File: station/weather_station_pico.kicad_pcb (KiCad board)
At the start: 2 copper layers, 75.1 x 75 mm, 24 parts, among them J2 STEMMA_QT, J3 73412-0110, J4 STEMMA, J5 RJ11, J6 RJ11, J7 DS18B20, J8 Battery Charger, U1 Pico, U2 RFM69, U3 APDS_LightSensor

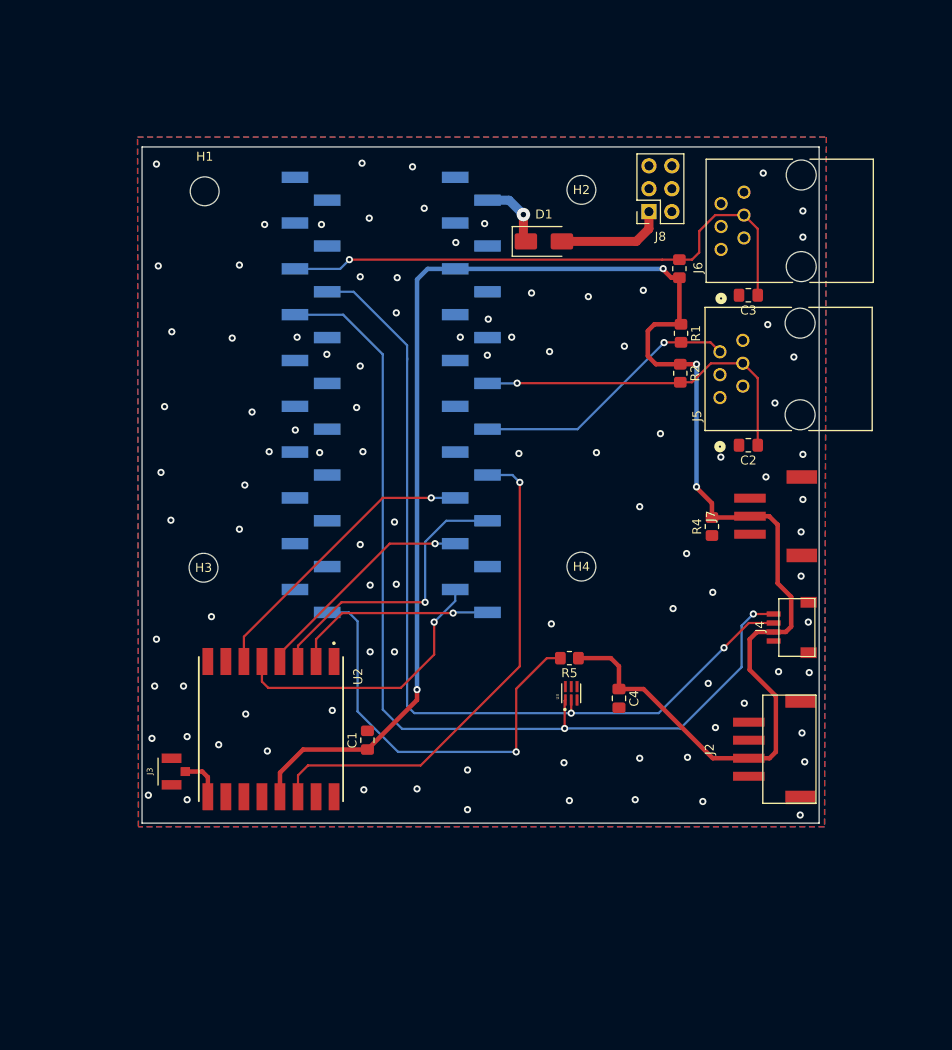
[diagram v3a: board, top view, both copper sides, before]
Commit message: Switched to a round board
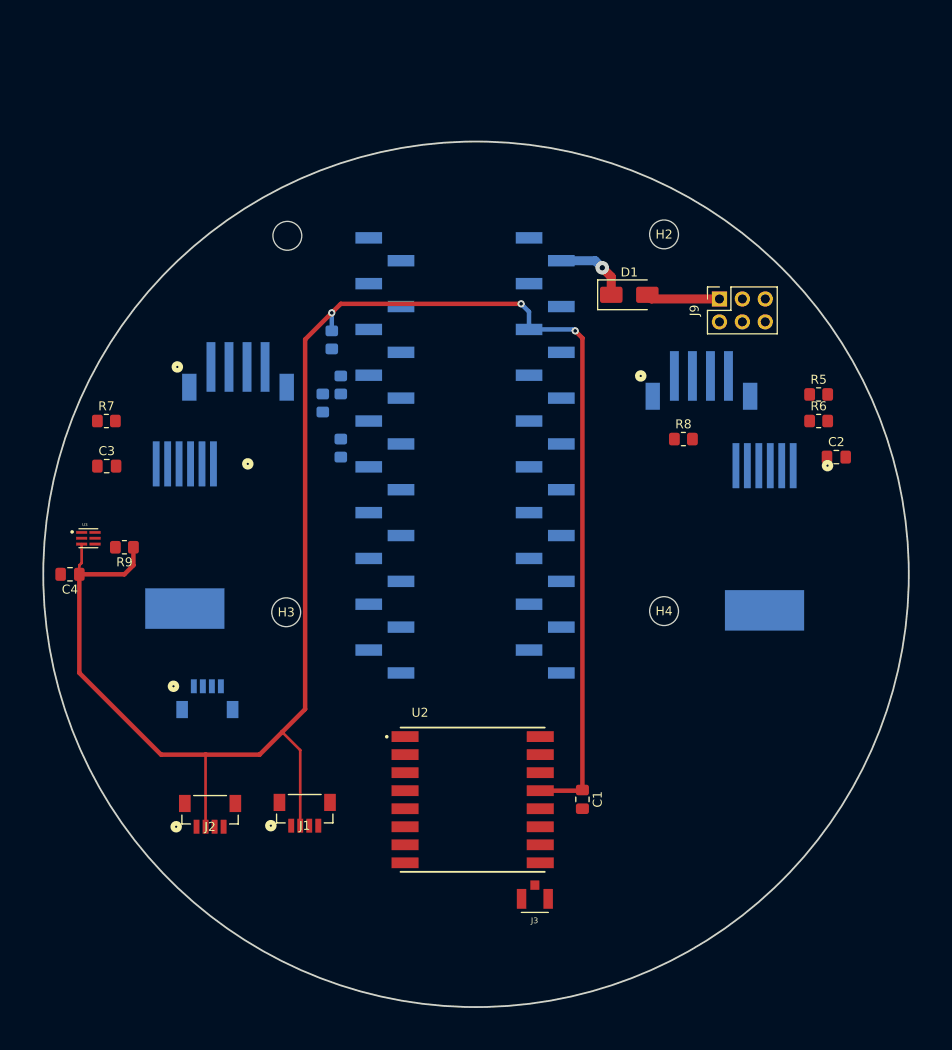
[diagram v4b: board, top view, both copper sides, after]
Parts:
- added J1: I2C1_EXP, WeatherStation:StemmaQT_Vertical, F.Cu at (128.4, 132.9)
- added J9: Battery Charger, Connector_PinSocket_2.54mm:PinSocket_2x03_P2.54mm_Vertical, F.Cu at (174.4, 76.4)
- added R6: 10K, Resistor_SMD:R_0805_2012Metric_Pad1.20x1.40mm_HandSolder, F.Cu at (185.4, 89.9)
- added R7: 10K, Resistor_SMD:R_0805_2012Metric_Pad1.20x1.40mm_HandSolder, F.Cu at (106.4, 89.9)
- added R8: 4.7k, Resistor_SMD:R_0805_2012Metric_Pad1.20x1.40mm_HandSolder, F.Cu at (170.4, 91.9)
- added R9: 10k, Resistor_SMD:R_0805_2012Metric_Pad1.20x1.40mm_HandSolder, F.Cu at (108.4, 103.9)
- J2: value STEMMA_QT -> I2C1_EXP; footprint WeatherStation:STEMMA_LARGE -> WeatherStation:StemmaQT_Vertical
- J4: value STEMMA -> BME280; footprint WeatherStation:STEMMA_SMALL -> WeatherStation:StemmaQT_Vertical; moved to B.Cu
- J5: value RJ11 -> WIND_SENSOR; footprint WeatherStation:CONN6_5555165-1_TEC -> WeatherStation:RJ11_SMD; moved to B.Cu
- J6: value RJ11 -> RAIN_SENSOR; footprint WeatherStation:CONN6_5555165-1_TEC -> WeatherStation:RJ11_SMD; moved to B.Cu
- J7: value DS18B20 -> SOIL_MOISTURE; footprint WeatherStation:STEMMA_LARGE_3pin -> WeatherStation:Stemma_Vertical_Large; moved to B.Cu
- J8: value Battery Charger -> SOIL_TEMP; footprint Connector_PinSocket_2.54mm:PinSocket_2x03_P2.54mm_Vertical -> WeatherStation:Stemma_Vertical_Large; moved to B.Cu
- R1, R2, R3: value 10K -> DNP; moved to B.Cu
- R4: value 4.7k -> DNP; moved to B.Cu
- R5: value 10k -> 10K
- U3: value APDS_LightSensor -> LIGHT_SENSOR
- moved C3 73.6 mm to (106.5, 94.9), turned to 0 degrees
- moved J6 67.4 mm to (115.1, 102.5), turned to 180 degrees
- moved J4 64.1 mm to (117.6, 121.2), turned to 0 degrees
- moved C4 62.4 mm to (102.4, 106.9), turned to 180 degrees
- moved J2 61.9 mm to (117.9, 133.0), turned to 0 degrees
- moved J7 60.5 mm to (121.0, 85.2), turned to 180 degrees
- moved U3 56.2 mm to (104.4, 102.9), turned to 0 degrees
- moved J3 42.7 mm to (154.0, 142.9), turned to 180 degrees
- moved R3 42.3 mm to (130.4, 87.9), turned to -90 degrees
- moved R4 42.1 mm to (132.4, 92.9)
- moved R5 40.2 mm to (185.4, 87.0), turned to 0 degrees
- moved R1 38.7 mm to (131.4, 80.9)
- moved R2 37.7 mm to (132.4, 85.9), turned to 90 degrees
- moved C1 24.7 mm to (159.2, 131.9), turned to -90 degrees
- moved U2 23.7 mm to (147.1, 131.9), turned to 0 degrees
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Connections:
- J2 pad 3: /I2C1_SDA -> /I2C0_SDA
- J2 pad 4: /I2C1_SCL -> /I2C0_SCL
- J2 pad 5: GND -> (no net)
- J2 pad 6: GND -> (no net)
- J3 pad 3: GND -> (no net)
- J4 pad 5: GND -> (no net)
- J4 pad 6: GND -> (no net)
- J7 pad 1: /ONE_WIRE -> GND
- J7 pad 3: GND -> /I2C0_SDA
- J7 pad 4: GND -> /I2C0_SCL
- J7 pad 5: GND -> (no net)
- J8 pad 1: /Battery Charger/Load+ -> /ONE_WIRE
- J8 pad 2: GND -> +3.3V
- J8 pad 4: /Battery Charger/SET -> (no net)
- J8 pad 5: /Battery Charger/~{FAULT} -> (no net)
- J8 pad 6: /Battery Charger/~{CHRG} -> (no net)
- R1 pad 2: /WINDDIR_OUT -> /I2C0_SDA
- R2 pad 2: /WINDSPEED_TGR -> /I2C0_SCL
- R3 pad 2: /RAIN_COUNT -> /I2C1_SDA
- R4 pad 1: /ONE_WIRE -> +3.3V
- R4 pad 2: +3.3V -> /I2C1_SCL
- R5 pad 2: /LIGHT_INTR -> /WINDDIR_OUT
- U1 pad 10: unconnected-(U1-GP7-Pad10) -> /I2C1_SCL
- U1 pad 19: unconnected-(U1-GP14-Pad19) -> /ONE_WIRE
- U1 pad 9: unconnected-(U1-GP6-Pad9) -> /I2C1_SDA
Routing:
- net /I2C0_SCL: track 106.4 -> 0.00 mm, vias 2 -> 0
- net /I2C0_SDA: track 98.2 -> 0.00 mm, vias 2 -> 0
- net /RAIN_COUNT: track 63.3 -> 0.00 mm, vias 1 -> 0
- net /RFM69 Radio/RFM69_INTR: track 56.3 -> 0.00 mm, vias 1 -> 0
- net /LIGHT_INTR: track 46.5 -> 0.00 mm, vias 1 -> 0
- net /WINDSPEED_TGR: track 39.0 -> 0.00 mm, vias 1 -> 0
- net /RFM69 Radio/RFM69_RESET: track 32.6 -> 0.00 mm, vias 1 -> 0
- net /RFM69 Radio/RFM69_MOSI: track 32.4 -> 0.00 mm, vias 1 -> 0
- net /RFM69 Radio/RFM69_CS: track 31.9 -> 0.00 mm, vias 1 -> 0
- net /WINDDIR_OUT: track 30.2 -> 0.00 mm, vias 1 -> 0
- net /RFM69 Radio/RFM69_CLK: track 25.4 -> 0.00 mm, vias 1 -> 0
- net /RFM69 Radio/RFM69_MISO: track 22.7 -> 0.00 mm, vias 1 -> 0
- net +3.3V: track 200.3 -> 206.2 mm, vias 4 -> 3
- net Net-(U2-ANT): track 4.93 -> 0.00 mm
- net /Battery Charger/Load+: track 12.1 -> 8.19 mm
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- removed copper zone on B.Cu, net GND
- removed copper zone on F.Cu, net GND
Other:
- board size 75.1 x 75 mm -> 96 x 96 mm

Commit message: Finished Circular Layout
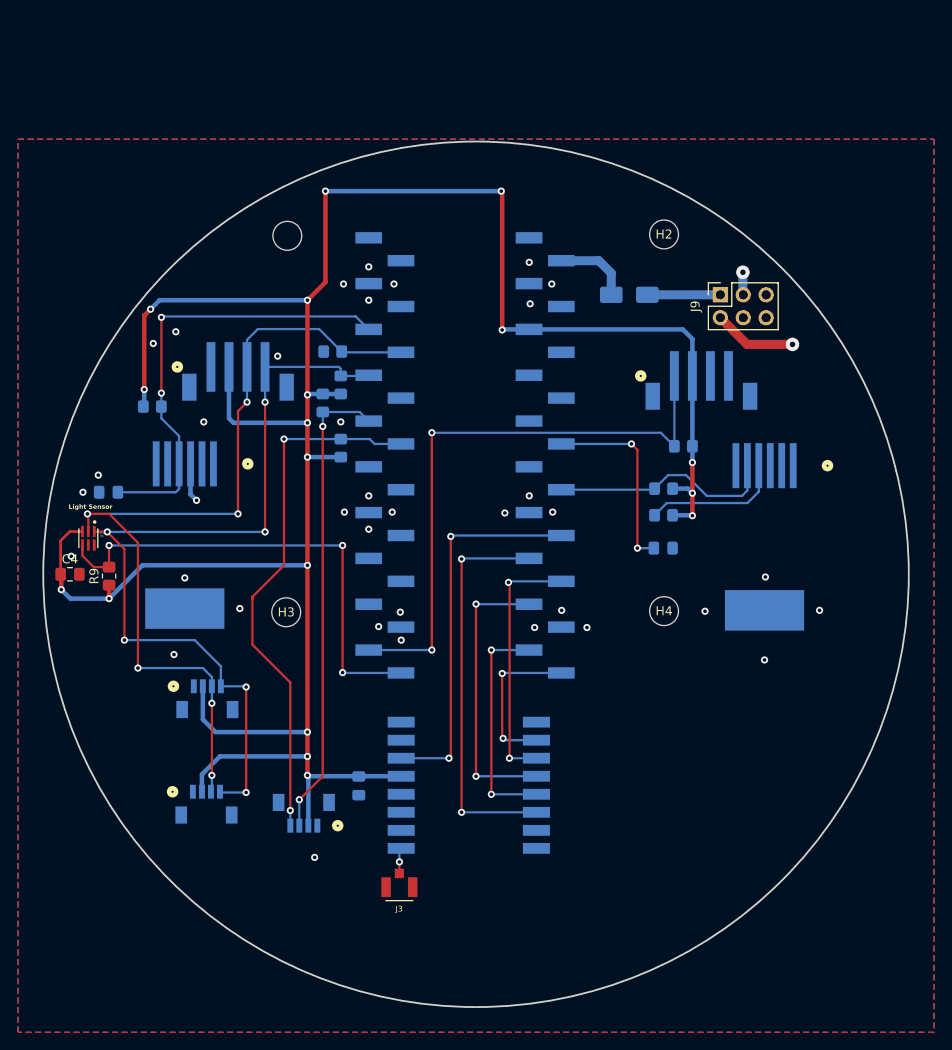
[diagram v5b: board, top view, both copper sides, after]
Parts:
- C1, C2, C3, D1, J1, R5, R6, R7, R8, U2: moved to B.Cu
- J2: value I2C1_EXP -> I2C0_EXP; moved to B.Cu
- moved C1 24.8 mm to (134.4, 130.4)
- moved C2 21.7 mm to (168.2, 104.0)
- moved R5 20.1 mm to (168.2, 97.4), turned to 180 degrees
- moved R6 20.1 mm to (168.2, 100.3), turned to 180 degrees
- moved J3 15.1 mm to (138.9, 141.6)
- moved R7 5.35 mm to (111.5, 88.3)
- moved R9 3.62 mm to (106.7, 107.1), turned to 90 degrees
- moved C3 2.91 mm to (106.7, 97.8), turned to 180 degrees
- moved U2 1.66 mm to (146.6, 130.3), turned to 180 degrees
- moved R1 1.30 mm to (131.5, 82.2), turned to 0 degrees
- moved R8 0.80 mm to (170.4, 92.7)
- moved J9 0.47 mm to (174.5, 75.9)
- moved J2 0.42 mm to (117.5, 132.9)
- moved J1 0.10 mm to (128.3, 132.9), turned to 180 degrees
- turned C4 to 0 degrees
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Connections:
- J1 pad 5: (no net) -> GND
- J1 pad 6: (no net) -> GND
- J2 pad 5: (no net) -> GND
- J2 pad 6: (no net) -> GND
- J3 pad 3: (no net) -> GND
- J4 pad 5: (no net) -> GND
- J4 pad 6: (no net) -> GND
- J5 pad 7: (no net) -> GND
- J6 pad 7: (no net) -> GND
- J8 pad 5: (no net) -> GND
- J8 pad 6: (no net) -> GND
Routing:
- net /I2C0_SDA: track 0.00 -> 99.3 mm, vias 0 -> 6
- net /I2C0_SCL: track 0.00 -> 94.1 mm, vias 0 -> 6
- net +3.3V: track 206.2 -> 282.6 mm, vias 3 -> 18
- net /ONE_WIRE: track 0.00 -> 66.4 mm, vias 0 -> 2
- net /I2C1_SCL: track 0.00 -> 59.3 mm, vias 0 -> 2
- net /LIGHT_INTR: track 0.00 -> 53.6 mm, vias 0 -> 3
- net /I2C1_SDA: track 0.00 -> 52.5 mm, vias 0 -> 2
- net /RAIN_COUNT: track 0.00 -> 50.4 mm, vias 0 -> 2
- net /RFM69 Radio/RFM69_RESET: track 0.00 -> 43.9 mm, vias 0 -> 2
- net /RFM69 Radio/RFM69_INTR: track 0.00 -> 42.3 mm, vias 0 -> 2
- net /WINDSPEED_TGR: track 0.00 -> 37.0 mm, vias 0 -> 2
- net /RFM69 Radio/RFM69_CLK: track 0.00 -> 31.7 mm, vias 0 -> 2
- net /RFM69 Radio/RFM69_MOSI: track 0.00 -> 28.5 mm, vias 0 -> 2
- net /WINDDIR_OUT: track 0.00 -> 25.3 mm
- net /RFM69 Radio/RFM69_CS: track 0.00 -> 25.2 mm, vias 0 -> 2
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- added copper zone on B.Cu, net GND
- added copper zone on F.Cu, net GND
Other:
- board text added: "Light Sensor"

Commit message: Finished Square layout
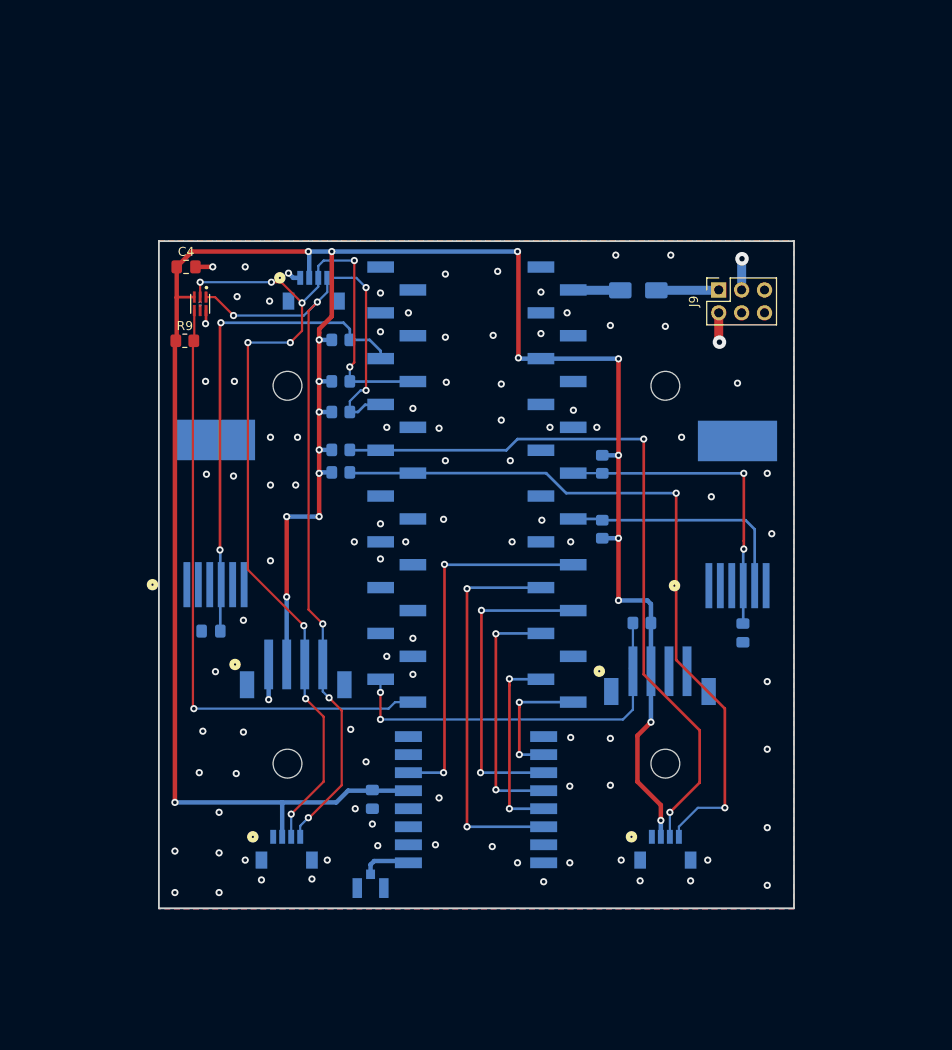
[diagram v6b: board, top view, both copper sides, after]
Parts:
- J3: moved to B.Cu
- moved H2 58.7 mm to (168.4, 127.9)
- moved H1 58.5 mm to (126.5, 127.9)
- moved J4 46.8 mm to (129.4, 75.9)
- moved J1 40.4 mm to (168.4, 137.9), turned to 0 degrees
- moved C4 36.4 mm to (115.3, 72.8)
- moved J7 33.6 mm to (127.4, 118.2)
- moved J8 33.1 mm to (167.8, 118.9)
- moved U3 28.8 mm to (116.8, 76.9)
- moved R9 27.4 mm to (115.1, 81.0), turned to 0 degrees
- moved H3 25.1 mm to (126.5, 86.0)
- moved H4 25.0 mm to (168.4, 86.0)
- moved R7 22.2 mm to (132.4, 80.9)
- moved R8 20.1 mm to (165.8, 112.3)
- moved C3 19.1 mm to (118.0, 113.2)
- moved C2 12.9 mm to (177.0, 113.4), turned to -90 degrees
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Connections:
- J1 pad 5: GND -> (no net)
- J1 pad 6: GND -> (no net)
- J2 pad 5: GND -> (no net)
- J2 pad 6: GND -> (no net)
- J3 pad 3: GND -> (no net)
- J4 pad 5: GND -> (no net)
- J4 pad 6: GND -> (no net)
- J5 pad 7: GND -> (no net)
- J6 pad 7: GND -> (no net)
- J8 pad 5: GND -> (no net)
- J8 pad 6: GND -> (no net)
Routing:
- net /I2C1_SDA: track 52.5 -> 81.2 mm
- net /ONE_WIRE: track 66.4 -> 43.0 mm
- net /I2C1_SCL: track 59.3 -> 81.4 mm
- net /LIGHT_INTR: track 53.6 -> 68.9 mm, vias 3 -> 1
- net /I2C0_SDA: track 99.3 -> 113.0 mm, vias 6 -> 10
- net /I2C0_SCL: track 94.1 -> 103.6 mm, vias 6 -> 7
- net +3.3V: track 282.6 -> 275.2 mm, vias 18 -> 19
- net /RFM69 Radio/RFM69_MOSI: track 28.5 -> 35.2 mm
- net /RAIN_COUNT: track 50.4 -> 54.8 mm
- net /RFM69 Radio/RFM69_CLK: track 31.7 -> 27.7 mm
- net /RFM69 Radio/RFM69_CS: track 25.2 -> 21.7 mm
- net Net-(D1-K): track 8.51 -> 5.24 mm
- net /RFM69 Radio/RFM69_MISO: track 17.6 -> 14.5 mm
- net Net-(U2-ANT): track 2.86 -> 5.52 mm, vias 1 -> 0
- net /WINDDIR_OUT: track 25.3 -> 26.9 mm
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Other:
- board size 96 x 96 mm -> 70.4 x 74 mm
- board text removed: "Light Sensor"

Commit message: Updated the I2C schematic for the soil moisture sensor
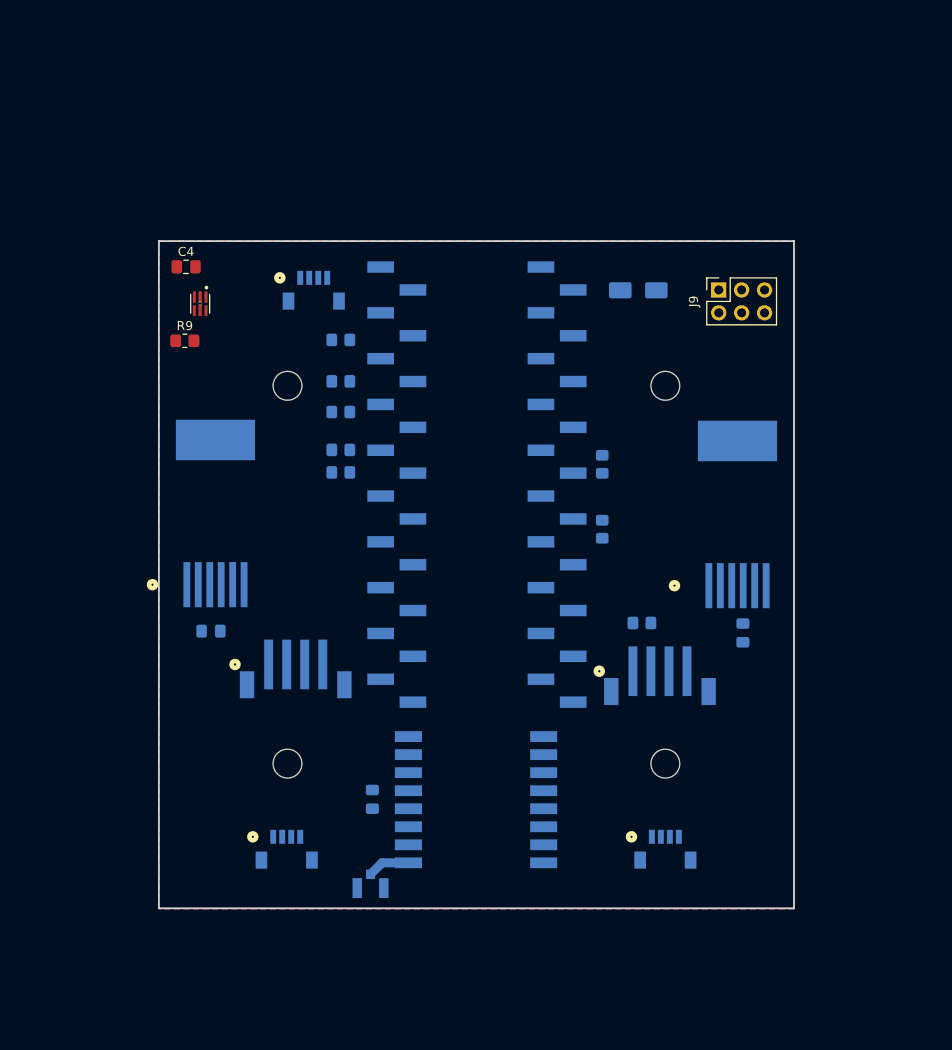
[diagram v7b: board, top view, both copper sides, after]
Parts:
- J8: value SOIL_TEMP -> SOIL_MOISTURE
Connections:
- J7 pad 1: GND -> /I2C0_SCL
- J7 pad 2: +3.3V -> /I2C0_SDA
- J7 pad 3: /I2C0_SDA -> +3.3V
- J7 pad 4: /I2C0_SCL -> GND
- J8 pad 1: /ONE_WIRE -> unconnected-(J8-Pin_1-Pad1)
- J8 pad 2: +3.3V -> /ONE_WIRE
- J8 pad 3: GND -> +3.3V
- J8 pad 4: (no net) -> GND
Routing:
- net +3.3V: track 275.2 -> 0.00 mm, vias 19 -> 0
- net /I2C0_SDA: track 113.0 -> 0.00 mm, vias 10 -> 0
- net /I2C0_SCL: track 103.6 -> 0.00 mm, vias 7 -> 0
- net /I2C1_SCL: track 81.4 -> 0.00 mm, vias 2 -> 0
- net /I2C1_SDA: track 81.2 -> 0.00 mm, vias 2 -> 0
- net /LIGHT_INTR: track 68.9 -> 0.00 mm, vias 1 -> 0
- net /RAIN_COUNT: track 54.8 -> 0.00 mm, vias 2 -> 0
- net /RFM69 Radio/RFM69_RESET: track 43.1 -> 0.00 mm, vias 2 -> 0
- net /ONE_WIRE: track 43.0 -> 0.00 mm, vias 2 -> 0
- net /RFM69 Radio/RFM69_INTR: track 41.3 -> 0.00 mm, vias 2 -> 0
- net /WINDSPEED_TGR: track 35.9 -> 0.00 mm, vias 2 -> 0
- net /RFM69 Radio/RFM69_MOSI: track 35.2 -> 0.00 mm, vias 2 -> 0
- net /RFM69 Radio/RFM69_CLK: track 27.7 -> 0.00 mm, vias 2 -> 0
- net /WINDDIR_OUT: track 26.9 -> 0.00 mm
- net /RFM69 Radio/RFM69_CS: track 21.7 -> 0.00 mm, vias 2 -> 0
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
